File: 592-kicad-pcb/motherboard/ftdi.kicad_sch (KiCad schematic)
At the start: 54 parts, among them J18 USB_B_Micro, U11 FT4232H, U12 74HC595, Y3 X322512MSB4SI

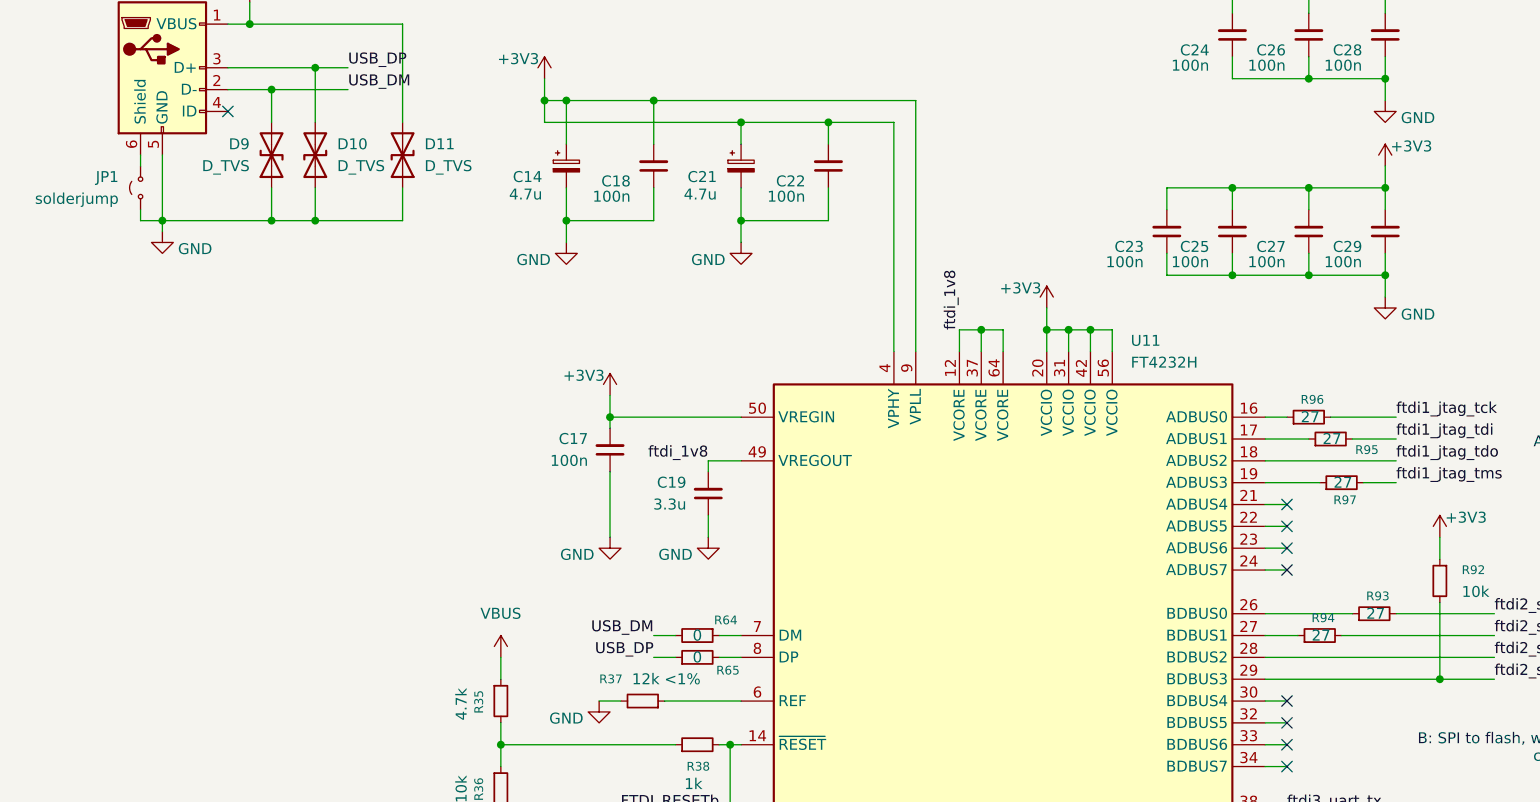
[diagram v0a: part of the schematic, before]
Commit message: update jlcpcb part numbers
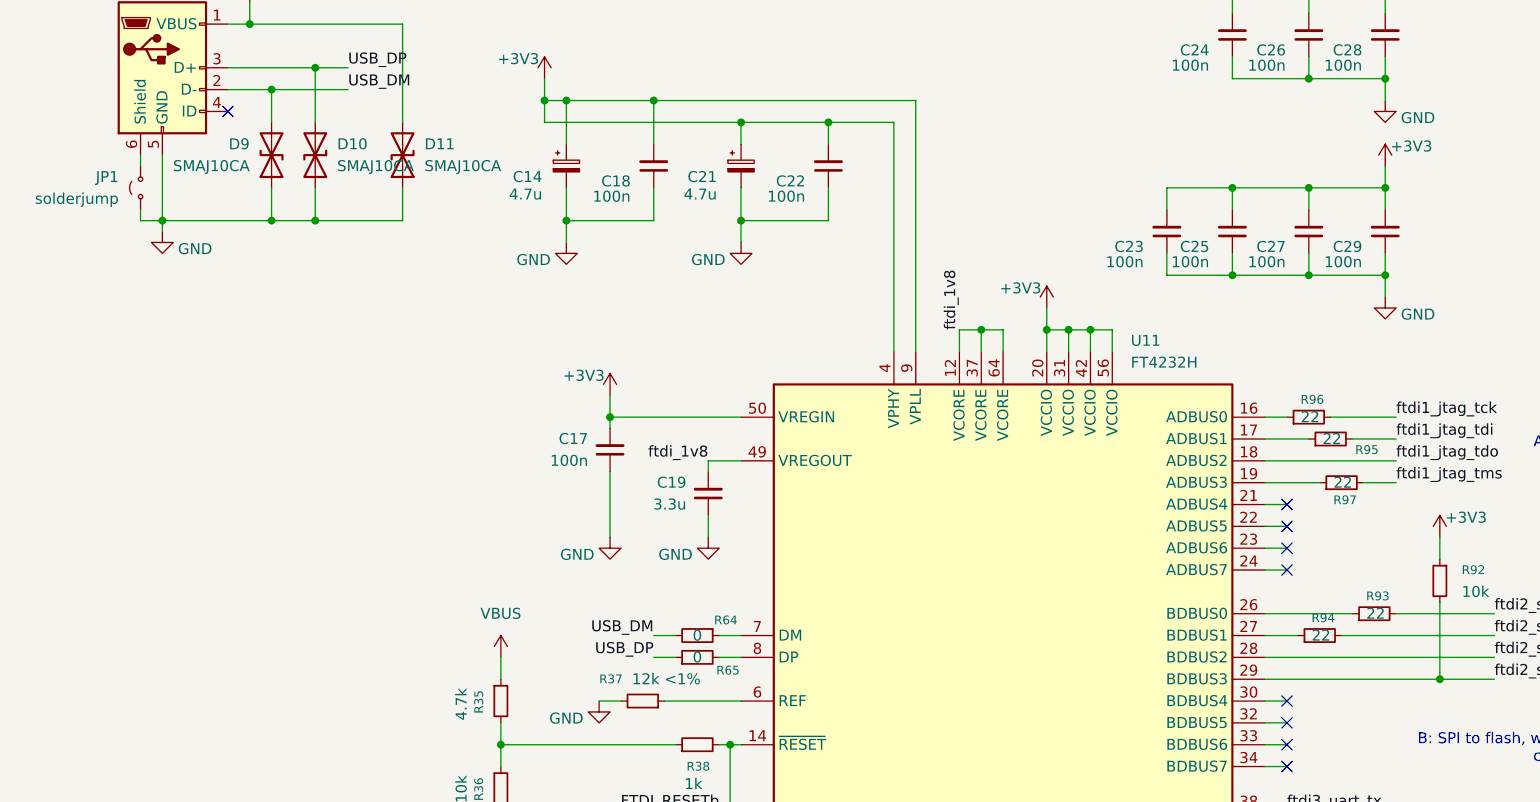
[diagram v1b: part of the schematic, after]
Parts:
- D10, D11, D9: value D_TVS -> SMAJ10CA; footprint (none) -> Diode_SMD:D_SMA; LCSC (none) -> C78398
- R64, R65: LCSC (none) -> C17168
- R92: footprint (none) -> Resistor_SMD:R_0402_1005Metric
- R93, R94, R95, R96, R97: value 27 -> 22; footprint (none) -> Resistor_SMD:R_0402_1005Metric; LCSC (none) -> C25092
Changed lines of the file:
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@@
 			)
 		)
-		(property "Value" "27"
+		(property "Value" "22"
 			(at 163.83 72.39 90)
 			(effects
@@
 			)
 		)
-		(property "Footprint" ""
+		(property "Footprint" "Resistor_SMD:R_0402_1005Metric"
 			(at 162.56 72.39 0)
 			(effects
@@
 			)
 		)
+		(property "LCSC" "C25092"
+			(at 162.56 72.39 90)
+			(effects
+				(font
+					(size 1.27 1.27)
+				)
+				(hide yes)
+			)
+		)
 		(pin "1"
 		)
@@
 			)
 		)
-		(property "Value" "27"
+		(property "Value" "22"
 			(at 161.29 69.85 90)
 			(effects
@@
 			)
 		)
-		(property "Footprint" ""
+		(property "Footprint" "Resistor_SMD:R_0402_1005Metric"
 			(at 160.02 69.85 0)
 			(effects
@@
 			)
 		)
+		(property "LCSC" "C25092"
+			(at 160.02 69.85 90)
+			(effects
+				(font
+					(size 1.27 1.27)
+				)
+				(hide yes)
+			)
+		)
 		(pin "1"
 		)
@@
 			)
 		)
-		(property "Value" "D_TVS"
+		(property "Value" "SMAJ10CA"
 			(at 57.15 40.6399 90)
 			(effects
@@
 			)
 		)
-		(property "Footprint" ""
+		(property "Footprint" "Diode_SMD:D_SMA"
 			(at 54.61 39.37 0)
 			(effects
@@
 			)
 		)
+		(property "LCSC" "C78398"
+			(at 54.61 39.37 90)
+			(effects
+				(font
+					(size 1.27 1.27)
+				)
+				(hide yes)
+			)
+		)
 		(pin "2"
 		)
@@
 			)
 		)
-		(property "Value" "27"
+		(property "Value" "22"
 			(at 165.1 77.47 90)
 			(effects
@@
 			)
 		)
-		(property "Footprint" ""
+		(property "Footprint" "Resistor_SMD:R_0402_1005Metric"
 			(at 163.83 77.47 0)
 			(effects
@@
 			)
 		)
+		(property "LCSC" "C25092"
+			(at 163.83 77.47 90)
+			(effects
+				(font
+					(size 1.27 1.27)
+				)
+				(hide yes)
+			)
+		)
 		(pin "1"
 		)
@@
 			)
 		)
-		(property "LCSC" ""
+		(property "LCSC" "C17168"
 			(at 88.9 97.79 90)
 			(effects
@@
 			)
 		)
-		(property "Value" "D_TVS"
+		(property "Value" "SMAJ10CA"
 			(at 46.99 40.6399 90)
 			(effects
@@
 			)
 		)
-		(property "Footprint" ""
+		(property "Footprint" "Diode_SMD:D_SMA"
 			(at 44.45 39.37 0)
 			(effects
@@
 			)
 		)
+		(property "LCSC" "C78398"
+			(at 44.45 39.37 90)
+			(effects
+				(font
+					(size 1.27 1.27)
+				)
+				(hide yes)
+			)
+		)
 		(pin "2"
 		)
@@
 			)
 		)
-		(property "Value" "27"
+		(property "Value" "22"
 			(at 162.56 95.25 90)
 			(effects
@@
 			)
 		)
-		(property "Footprint" ""
+		(property "Footprint" "Resistor_SMD:R_0402_1005Metric"
 			(at 161.29 95.25 0)
 			(effects
@@
 			)
 		)
+		(property "LCSC" "C25092"
+			(at 161.29 95.25 90)
+			(effects
+				(font
+					(size 1.27 1.27)
+				)
+				(hide yes)
+			)
+		)
 		(pin "1"
 		)
@@
 			)
 		)
-		(property "Footprint" ""
+		(property "Footprint" "Resistor_SMD:R_0402_1005Metric"
 			(at 175.26 88.9 0)
 			(effects
@@
 			)
 		)
-		(property "Value" "D_TVS"
+		(property "Value" "SMAJ10CA"
 			(at 36.83 40.6399 90)
 			(effects
@@
 			)
 		)
-		(property "Footprint" ""
+		(property "Footprint" "Diode_SMD:D_SMA"
 			(at 39.37 39.37 0)
 			(effects
@@
 			)
 		)
+		(property "LCSC" "C78398"
+			(at 39.37 39.37 90)
+			(effects
+				(font
+					(size 1.27 1.27)
+				)
+				(hide yes)
+			)
+		)
 		(pin "2"
 		)
@@
 			)
 		)
-		(property "Value" "27"
+		(property "Value" "22"
 			(at 168.91 92.71 90)
 			(effects
@@
 			)
 		)
-		(property "Footprint" ""
+		(property "Footprint" "Resistor_SMD:R_0402_1005Metric"
 			(at 167.64 92.71 0)
 			(effects
@@
 			)
 		)
+		(property "LCSC" "C25092"
+			(at 167.64 92.71 90)
+			(effects
+				(font
+					(size 1.27 1.27)
+				)
+				(hide yes)
+			)
+		)
 		(pin "1"
 		)
@@
 			)
 		)
-		(property "LCSC" ""
+		(property "LCSC" "C17168"
 			(at 88.9 95.25 90)
 			(effects

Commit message: can't work on one machine
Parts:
- C21: now left out of the parts list
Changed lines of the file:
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@@
 		(unit 1)
 		(exclude_from_sim no)
-		(in_bom yes)
+		(in_bom no)
 		(on_board yes)
 		(dnp no)
